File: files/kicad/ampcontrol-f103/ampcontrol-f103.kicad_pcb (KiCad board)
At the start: 2 copper layers, 63 parts, among them J1 Audio, J10 Buttons, J11 Encoder, J12 SPI, J13 I2C_Audio, J14 I2C_Tuner, J15 I2C_Ext, J16 LCD_DATA, J17 LCD_CTRL, J2 MUTE_STBY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

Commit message: PCB arrangement
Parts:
- removed J17: LCD_CTRL, Connector_PinHeader_2.54mm:PinHeader_1x06_P2.54mm_Vertical
- added R20: 4.7k, Resistor_SMD:R_0805_2012Metric, F.Cu at (117.2, 86.5)
- BT1, J10, J11, J2, J4, J7, J9, RV1, RV2, SW1, Y1, Y2: moved to B.Cu
- C1: value 0.22 -> 2.2; footprint Capacitor_SMD:C_1206_3216Metric -> Capacitor_SMD:C_0805_2012Metric
- C10, C11, C12, C14, C3, C4, C5, C6, C7, C9: footprint Capacitor_SMD:C_1206_3216Metric -> Capacitor_SMD:C_0805_2012Metric
- C2: value 2.2 -> 0.22; footprint Capacitor_SMD:C_1206_3216Metric -> Capacitor_SMD:C_0805_2012Metric
- J1: value Audio -> SP; moved to B.Cu
- J12: value SPI -> LCD_CTRL; footprint Connector_PinHeader_2.54mm:PinHeader_1x04_P2.54mm_Vertical -> Connector_PinSocket_2.54mm:PinSocket_1x14_P2.54mm_Vertical
- J13: value I2C_Audio -> SPI; footprint Connector_PinHeader_2.54mm:PinHeader_1x04_P2.54mm_Vertical -> Connector_PinSocket_2.54mm:PinSocket_1x04_P2.54mm_Vertical
- J14: value I2C_Tuner -> I2C; footprint Connector_PinHeader_2.54mm:PinHeader_1x05_P2.54mm_Vertical -> Connector_PinHeader_2.54mm:PinHeader_1x04_P2.54mm_Vertical; moved to B.Cu
- J15: value I2C_Ext -> I2C; footprint Connector_PinHeader_2.54mm:PinHeader_1x04_P2.54mm_Vertical -> Connector_PinHeader_2.54mm:PinHeader_1x05_P2.54mm_Vertical; moved to B.Cu
- J16: value LCD_DATA -> I2C; footprint Connector_PinHeader_2.54mm:PinHeader_1x08_P2.54mm_Vertical -> Connector_PinHeader_2.54mm:PinHeader_1x04_P2.54mm_Vertical; moved to B.Cu
- J3: value UART -> UART1; footprint Connector_PinHeader_2.54mm:PinHeader_1x04_P2.54mm_Vertical -> Connector_PinHeader_2.54mm:PinHeader_1x03_P2.54mm_Vertical; moved to B.Cu
- J5, J6: footprint Connector_PinHeader_2.54mm:PinHeader_1x04_P2.54mm_Vertical -> Connector_PinHeader_2.54mm:PinHeader_1x03_P2.54mm_Vertical; moved to B.Cu
- J8: value BOOT -> LCD_DATA; footprint Connector_PinHeader_2.54mm:PinHeader_1x02_P2.54mm_Vertical -> Connector_PinSocket_2.54mm:PinSocket_1x08_P2.54mm_Vertical
- R1, R2, R22, R23, R3: footprint Resistor_SMD:R_1206_3216Metric -> Resistor_SMD:R_0805_2012Metric; moved to B.Cu
- R10, R11, R12, R13, R14, R15, R16, R17, R18, R19, R21, R4, R5, R6, R7, R8, R9: footprint Resistor_SMD:R_1206_3216Metric -> Resistor_SMD:R_0805_2012Metric
- moved R12 76.6 mm to (114.7, 113.8), turned to 90 degrees
- moved R15 72.0 mm to (124.2, 113.8), turned to 90 degrees
- moved Q1 69.7 mm to (115.7, 103.8), turned to 180 degrees
- moved R11 69.4 mm to (110.7, 106.8)
- moved R10 68.7 mm to (110.7, 102.8)
- moved R21 68.4 mm to (106.5, 103.9), turned to 180 degrees
- moved R13 66.2 mm to (117.9, 113.8), turned to 90 degrees
- moved J12 62.0 mm to (102.7, 83.6)
- moved R14 59.8 mm to (121.1, 113.8), turned to 90 degrees
- moved U2 57.6 mm to (134.3, 100.5), turned to 180 degrees
- moved R22 56.3 mm to (128.6, 93.1), turned to 90 degrees
- moved R23 53.7 mm to (131.2, 93.1), turned to 90 degrees
- moved J6 52.9 mm to (147.7, 118.5), turned to 90 degrees
- moved SW1 52.3 mm to (107.9, 91.0)
- moved J8 50.5 mm to (117.2, 109.3), turned to 90 degrees
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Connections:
- net Net-(J4-Pad2) renamed /USB_M
- net Net-(J4-Pad3) renamed /USB_P
- C1 pad 1: +3V3 -> Net-(C1-Pad1)
- C1 pad 2: GNDD -> Net-(C1-Pad2)
- C2 pad 1: Net-(C2-Pad1) -> +3V3
- C2 pad 2: Net-(C2-Pad2) -> GNDD
- J11 pad 1: /ENC_A -> /BTN_5
- J11 pad 3: /ENC_B -> /ENC_A
- J11 pad 5: /BTN_5 -> /ENC_B
- J12 pad 1: /SD_DO -> +3V3
- J12 pad 2: /SD_CLK -> GNDD
- J12 pad 3: /SD_DIN -> /CS
- J12 pad 4: /SD_CS -> /NRST
- J13 pad 1: +5V -> /SD_CS
- J13 pad 2: /SCL -> /SD_MOSI
- J13 pad 3: /SDA -> /SD_MISO
- J13 pad 4: GNDD -> /SD_SCK
- J14 pad 4: /HW_RST -> GNDD
- J15 pad 4: GNDD -> /HW_RST
- J16 pad 1: /DB0 -> +5V
- J16 pad 2: /DB1 -> /SCL
- J16 pad 3: /DB2 -> /SDA
- J16 pad 4: /DB3 -> GNDD
- J3 pad 1: +3V3 -> /TX1
- J3 pad 2: /TX -> /RX1
- J3 pad 3: /RX -> GNDD
- J5 pad 1: +3V3 -> /TX2
- J5 pad 2: /TX2 -> /RX2
- J5 pad 3: /RX2 -> GNDD
- J6 pad 1: +3V3 -> /TX3
- J6 pad 2: /TX3 -> /RX3
- J6 pad 3: /RX3 -> GNDD
- J8 pad 1: /BOOT0 -> /DB0
- J8 pad 2: GNDD -> /DB1
- R4 pad 1: Net-(C2-Pad1) -> Net-(C3-Pad1)
- R5 pad 1: Net-(C3-Pad1) -> Net-(C1-Pad1)
- RV1 pad 1: /IN_L -> /IN_R
- RV1 pad 2: Net-(C2-Pad2) -> Net-(C1-Pad2)
- RV2 pad 1: /IN_R -> /IN_L
- U2 pad 15: /SD_CLK -> /SD_SCK
- U2 pad 16: /SD_DO -> /SD_MISO
- U2 pad 17: /SD_DIN -> /SD_MOSI
- U2 pad 30: /TX -> /TX1
- U2 pad 31: /RX -> /RX1
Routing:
- net (no net): vias 0 -> 4
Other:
- board outline added: 77.2 x 42.7 mm

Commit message: Test PCB layout
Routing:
- net GNDD: track 0.00 -> 326.6 mm, vias 0 -> 2
- net +3V3: track 0.00 -> 224.3 mm
- net /MUTE: track 0.00 -> 85.7 mm, vias 0 -> 1
- net +5V: track 0.00 -> 83.1 mm
- net /STBY: track 0.00 -> 80.5 mm, vias 0 -> 1
- net /SD_SCK: track 0.00 -> 71.2 mm, vias 0 -> 1
- net /NRST: track 0.00 -> 70.3 mm, vias 0 -> 1
- net /SD_MOSI: track 0.00 -> 62.3 mm, vias 0 -> 1
- net /SCL: track 0.00 -> 61.8 mm, vias 0 -> 1
- net /USB_DP: track 0.00 -> 61.2 mm, vias 0 -> 1
- net /BOOT0: track 0.00 -> 57.0 mm
- net /SDA: track 0.00 -> 56.8 mm, vias 0 -> 1
- net /USB_DM: track 0.00 -> 53.1 mm, vias 0 -> 1
- net /BCKL: track 0.00 -> 44.9 mm, vias 0 -> 1
- net /RX1: track 0.00 -> 42.8 mm, vias 0 -> 1
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
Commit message: Universal PCB for ILI9341 PCB
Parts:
- added J13_2.8: SPI, Connector_PinSocket_2.54mm:PinSocket_1x04_P2.54mm_Vertical, F.Cu at (177.7, 77.3)
- added J13_3.2: SPI, Connector_PinSocket_2.54mm:PinSocket_1x04_P2.54mm_Vertical, F.Cu at (181.0, 77.3)
- moved R21 33.0 mm to (114.7, 72.0), turned to 270 degrees
- moved J1 19.9 mm to (155.7, 63.0)
- moved J15 19.9 mm to (130.2, 63.0)
- moved J3 19.9 mm to (140.4, 63.0)
- moved J5 19.9 mm to (150.6, 63.0)
- moved J7 19.9 mm to (115.0, 63.0)
- moved J11 19.9 mm to (126.5, 98.0)
- moved J14 19.9 mm to (127.7, 70.7)
- moved J16 19.9 mm to (127.7, 66.8)
- moved R17 19.9 mm to (124.6, 94.8)
- moved BT1 19.9 mm to (112.5, 80.8)
- moved C1 19.9 mm to (164.6, 70.9)
- moved C10 19.9 mm to (137.5, 75.7)
- moved C11 19.9 mm to (116.3, 84.3)
- moved C12 19.9 mm to (149.2, 88.4)
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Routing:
- net GNDD: track 326.6 -> 456.9 mm, vias 2 -> 12
- net /SD_CS: track 31.7 -> 65.0 mm
- net /TX1: track 27.2 -> 60.5 mm, vias 0 -> 1
- net /MUTE: track 85.7 -> 54.2 mm, vias 1 -> 0
- net /SD_MISO: track 32.4 -> 61.1 mm, vias 0 -> 1
- net /STBY: track 80.5 -> 55.1 mm, vias 1 -> 0
- net /SCL: track 61.8 -> 37.3 mm
- net /SDA: track 56.8 -> 32.6 mm
- net +3V3: track 224.3 -> 247.9 mm, vias 0 -> 3
- net /SD_MOSI: track 62.3 -> 84.4 mm, vias 1 -> 0
- net /SD_SCK: track 71.2 -> 57.7 mm
- net /NRST: track 70.3 -> 59.0 mm
- net /VBAT: track 23.2 -> 16.0 mm
- net /SCK: track 31.8 -> 37.3 mm, vias 1 -> 0
- net /RX1: track 42.8 -> 37.4 mm, vias 1 -> 0
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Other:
- board size 77.2 x 42.7 mm -> 89.3 x 55 mm

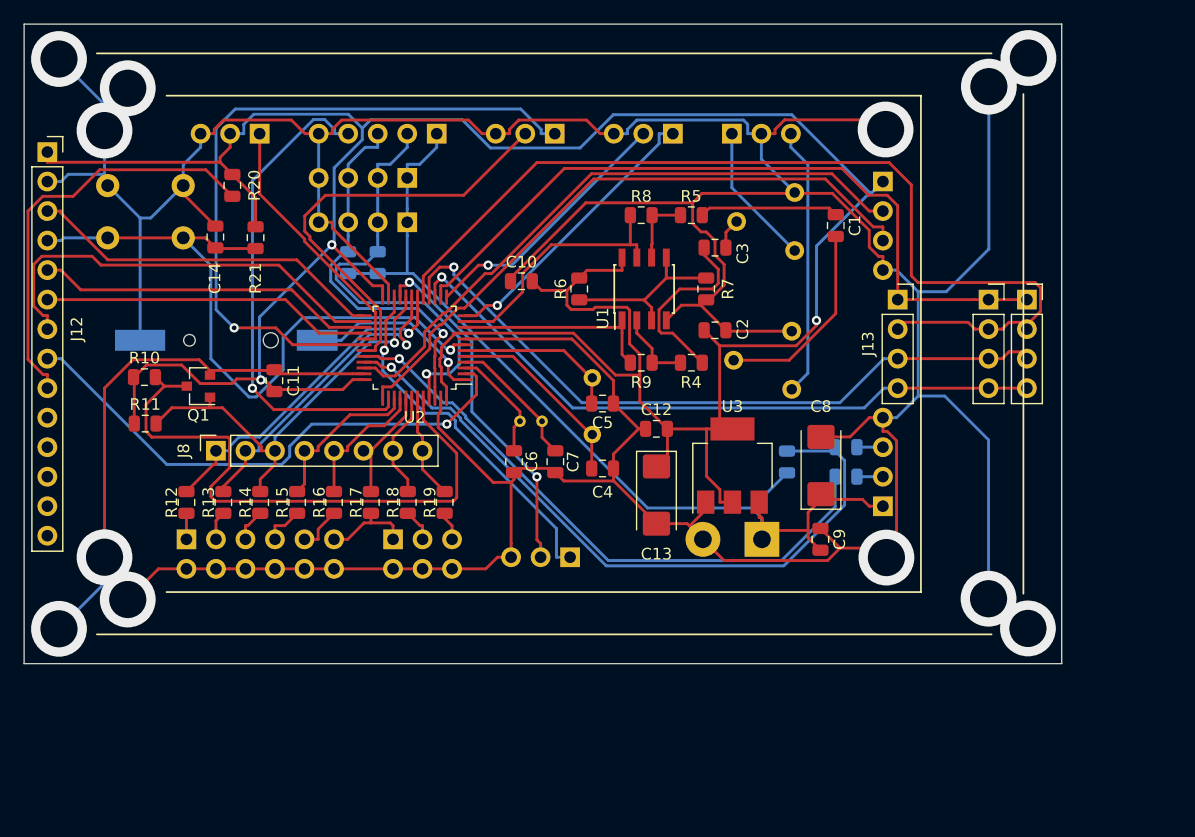
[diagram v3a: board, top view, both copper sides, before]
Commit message: Finish with ILI9341 SPI PCB
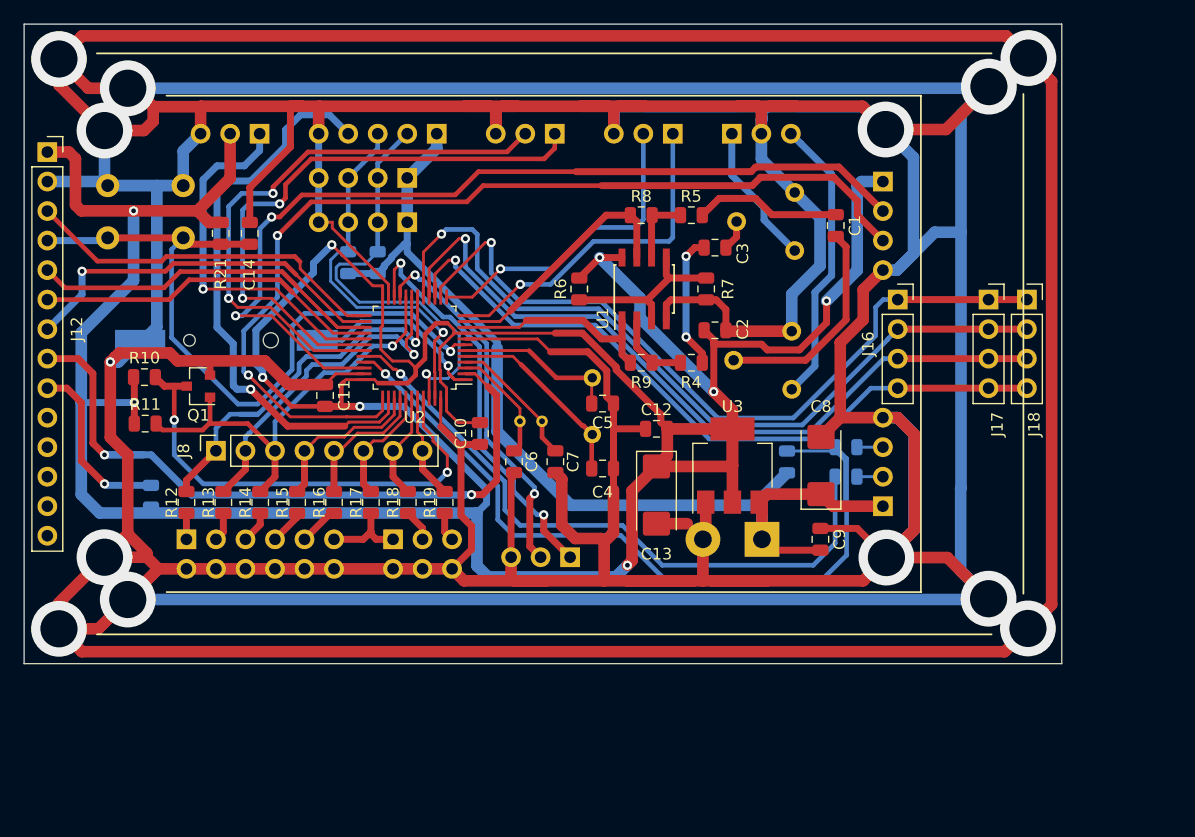
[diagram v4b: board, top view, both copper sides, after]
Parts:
- removed J13_2.8, J13_3.2: SPI, Connector_PinSocket_2.54mm:PinSocket_1x04_P2.54mm_Vertical
- added J17: SPI, Connector_PinSocket_2.54mm:PinSocket_1x04_P2.54mm_Vertical, F.Cu at (177.7, 77.3)
- added J18: SPI, Connector_PinSocket_2.54mm:PinSocket_1x04_P2.54mm_Vertical, F.Cu at (181.0, 77.3)
- R20: moved to B.Cu
- moved R20 27.7 mm to (105.7, 94.2), turned to 90 degrees
- moved C10 13.6 mm to (134.0, 88.8), turned to 90 degrees
- moved C11 4.54 mm to (120.6, 85.6)
- moved R21 3.02 mm to (111.7, 71.6)
- moved C14 2.98 mm to (114.2, 71.6)
- renumbered J14 to J13, J16 to J14, J13 to J16
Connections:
- net Net-(J12-Pad9) renamed /RD
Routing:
- net GNDD: track 456.9 -> 1039.4 mm, vias 12 -> 13
- net +3V3: track 247.9 -> 327.4 mm, vias 3 -> 9
- net /STBY: track 55.1 -> 85.5 mm, vias 0 -> 2
- net /MUTE: track 54.2 -> 79.0 mm, vias 0 -> 2
- net /RD: track 36.1 -> 15.3 mm, vias 0 -> 1
- net /BCKL: track 46.3 -> 62.5 mm, vias 1 -> 2
- net /SD_MOSI: track 84.4 -> 70.8 mm, vias 0 -> 1
- net Net-(R6-Pad2): track 15.5 -> 28.3 mm
- net /RX1: track 37.4 -> 49.9 mm, vias 0 -> 2
- net +5V: track 82.8 -> 95.3 mm
- net /HW_RST: track 42.3 -> 53.5 mm
- net /IR: track 22.8 -> 33.6 mm, vias 0 -> 1
- net /USB_DP: track 60.3 -> 70.9 mm
- net /TX1: track 60.5 -> 50.7 mm, vias 1 -> 2
- net /BOOT0: track 51.9 -> 43.0 mm, vias 0 -> 2
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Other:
- net class Power added: clearance 0.2, trace_width 0.25, via_dia 0.8, via_drill 0.4
- board text added: "https://github.com/ WiseLord/ampcontrol-f103"

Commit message: Add sockets for arduino-pinout displays
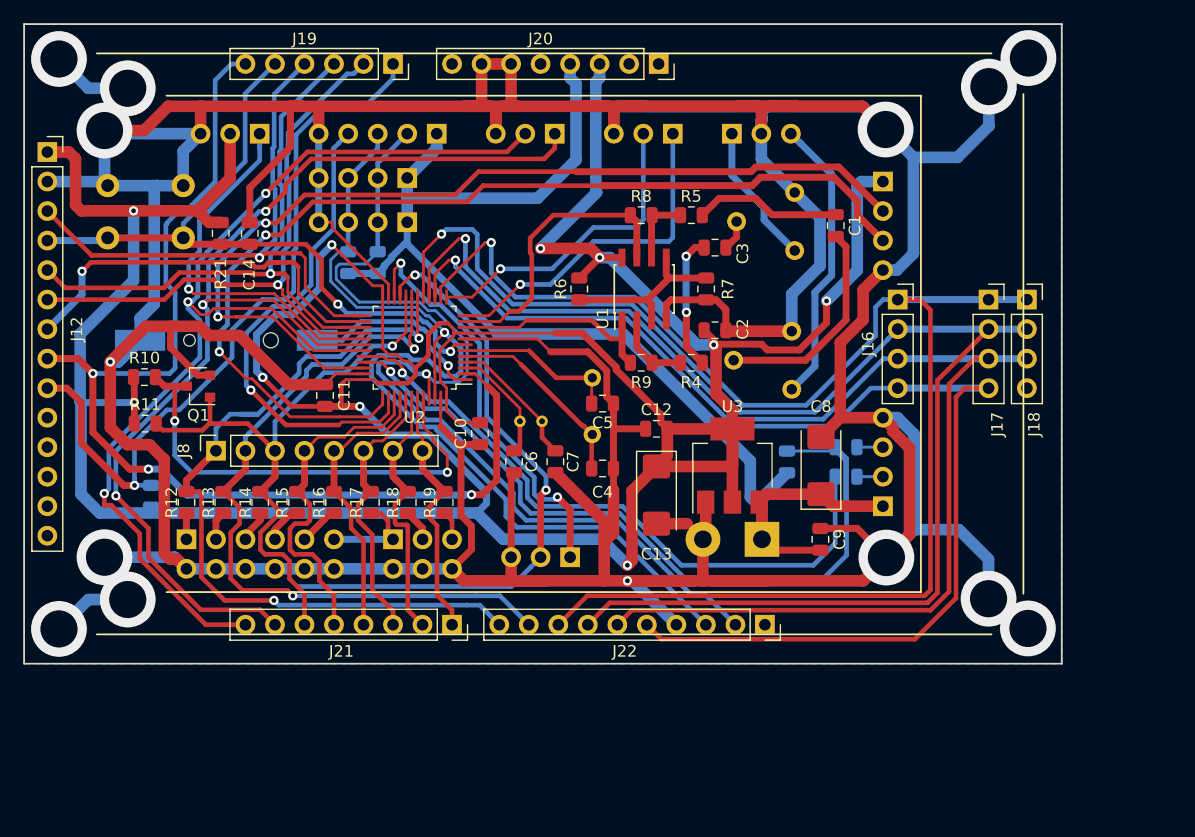
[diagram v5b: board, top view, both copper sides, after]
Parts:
- added J19: Arduino_Analog, Connector_PinSocket_2.54mm:PinSocket_1x06_P2.54mm_Vertical, F.Cu at (126.5, 57.0)
- added J20: Arduino_Power, Connector_PinSocket_2.54mm:PinSocket_1x08_P2.54mm_Vertical, F.Cu at (149.3, 57.0)
- added J21: Arduino_Digital_low, Connector_PinSocket_2.54mm:PinSocket_1x08_P2.54mm_Vertical, F.Cu at (131.6, 105.3)
- added J22: Arduino_Digital_High, Connector_PinSocket_2.54mm:PinSocket_1x10_P2.54mm_Vertical, F.Cu at (158.5, 105.3)
- J16: value SPI -> SPI_2.4
- J17: value SPI -> SPI_2.8
- J18: value SPI -> SPI_3.2
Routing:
- net GNDD: track 1039.4 -> 622.8 mm, vias 13 -> 14
- net /SD_CS: track 66.3 -> 126.0 mm
- net /SD_MOSI: track 70.8 -> 124.4 mm
- net /SDA: track 32.3 -> 85.3 mm
- net /SD_MISO: track 67.9 -> 118.9 mm
- net /RD: track 15.3 -> 63.8 mm
- net /SCL: track 37.3 -> 84.6 mm
- net /SD_SCK: track 64.3 -> 109.1 mm
- net /TX1: track 50.7 -> 95.1 mm, vias 2 -> 3
- net /RX1: track 49.9 -> 93.1 mm, vias 2 -> 3
- net /DB0: track 35.5 -> 71.2 mm, vias 1 -> 2
- net /DB1: track 31.1 -> 65.8 mm, vias 1 -> 2
- net /BCKL: track 62.5 -> 96.2 mm, vias 2 -> 3
- net /WR: track 29.9 -> 52.7 mm, vias 0 -> 1
- net /RX3: track 33.5 -> 55.5 mm
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- added copper zone on B.Cu, net GNDD
- added copper zone on F.Cu, net GNDD
